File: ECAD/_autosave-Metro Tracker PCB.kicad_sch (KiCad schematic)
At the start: 7 parts, among them IC1 FT230XS-R, IC2 LM1117MPX-3.3_NOPB

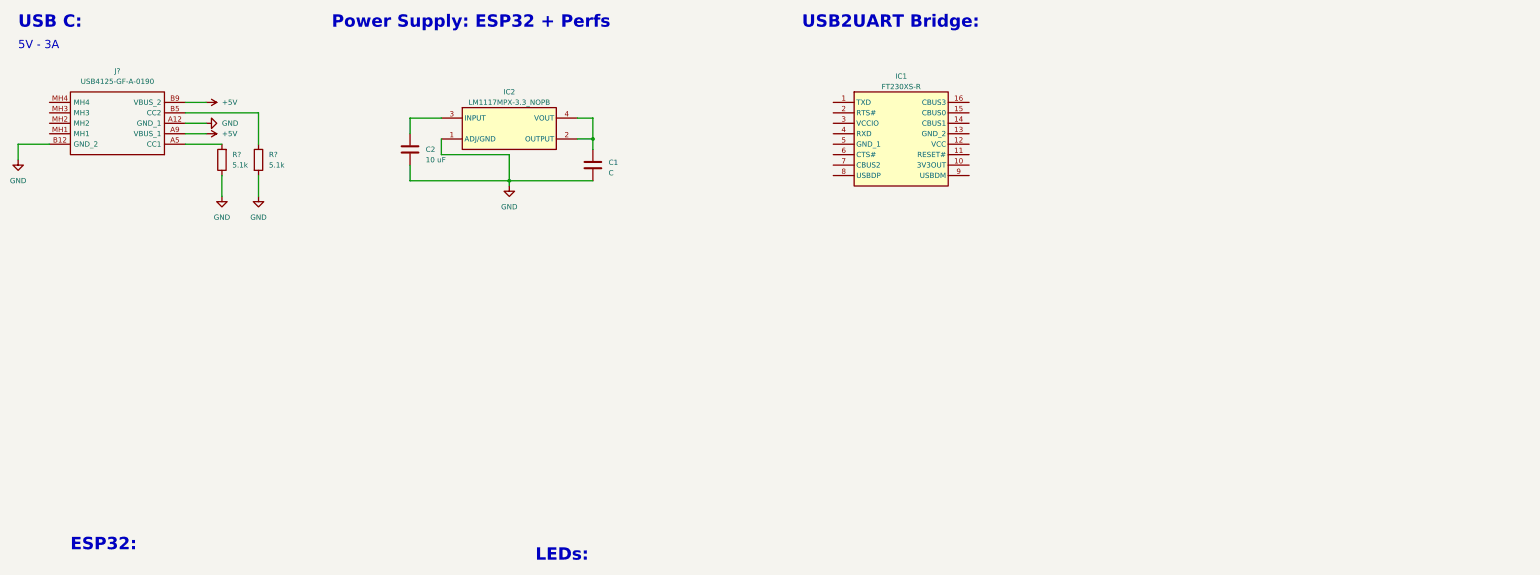
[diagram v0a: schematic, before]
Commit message: usb c bridge
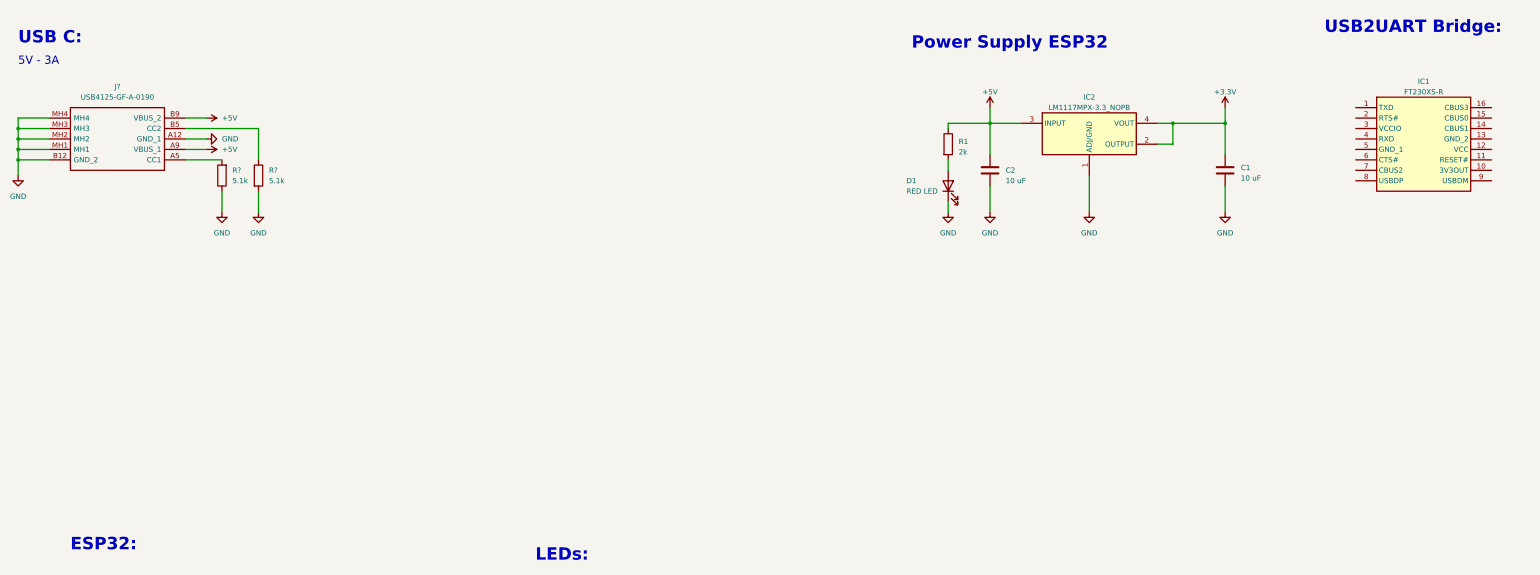
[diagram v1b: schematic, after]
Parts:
- added D1: RED LED, symbol Device:LED
- added R1: 2k, symbol Device:R
- C1: value C -> 10 uF
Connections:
- net +5V: now also C2.1, IC2.3 (INPUT), R1.1
- net GND: now also J?.MH1, J?.MH2, J?.MH3, J?.MH4, D1.1 (K)
- net +3.3V: now reaches C1.1, IC2.2 (OUTPUT), IC2.4 (VOUT)
- new net: D1.2 (A), R1.2
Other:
- note added: "Power Supply ESP32"
- note removed: "Power Supply: ESP32 + Perfs"
- moved on the sheet: C2, IC1, IC2, J?, R?
